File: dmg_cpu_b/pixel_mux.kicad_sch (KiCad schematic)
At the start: 50 parts

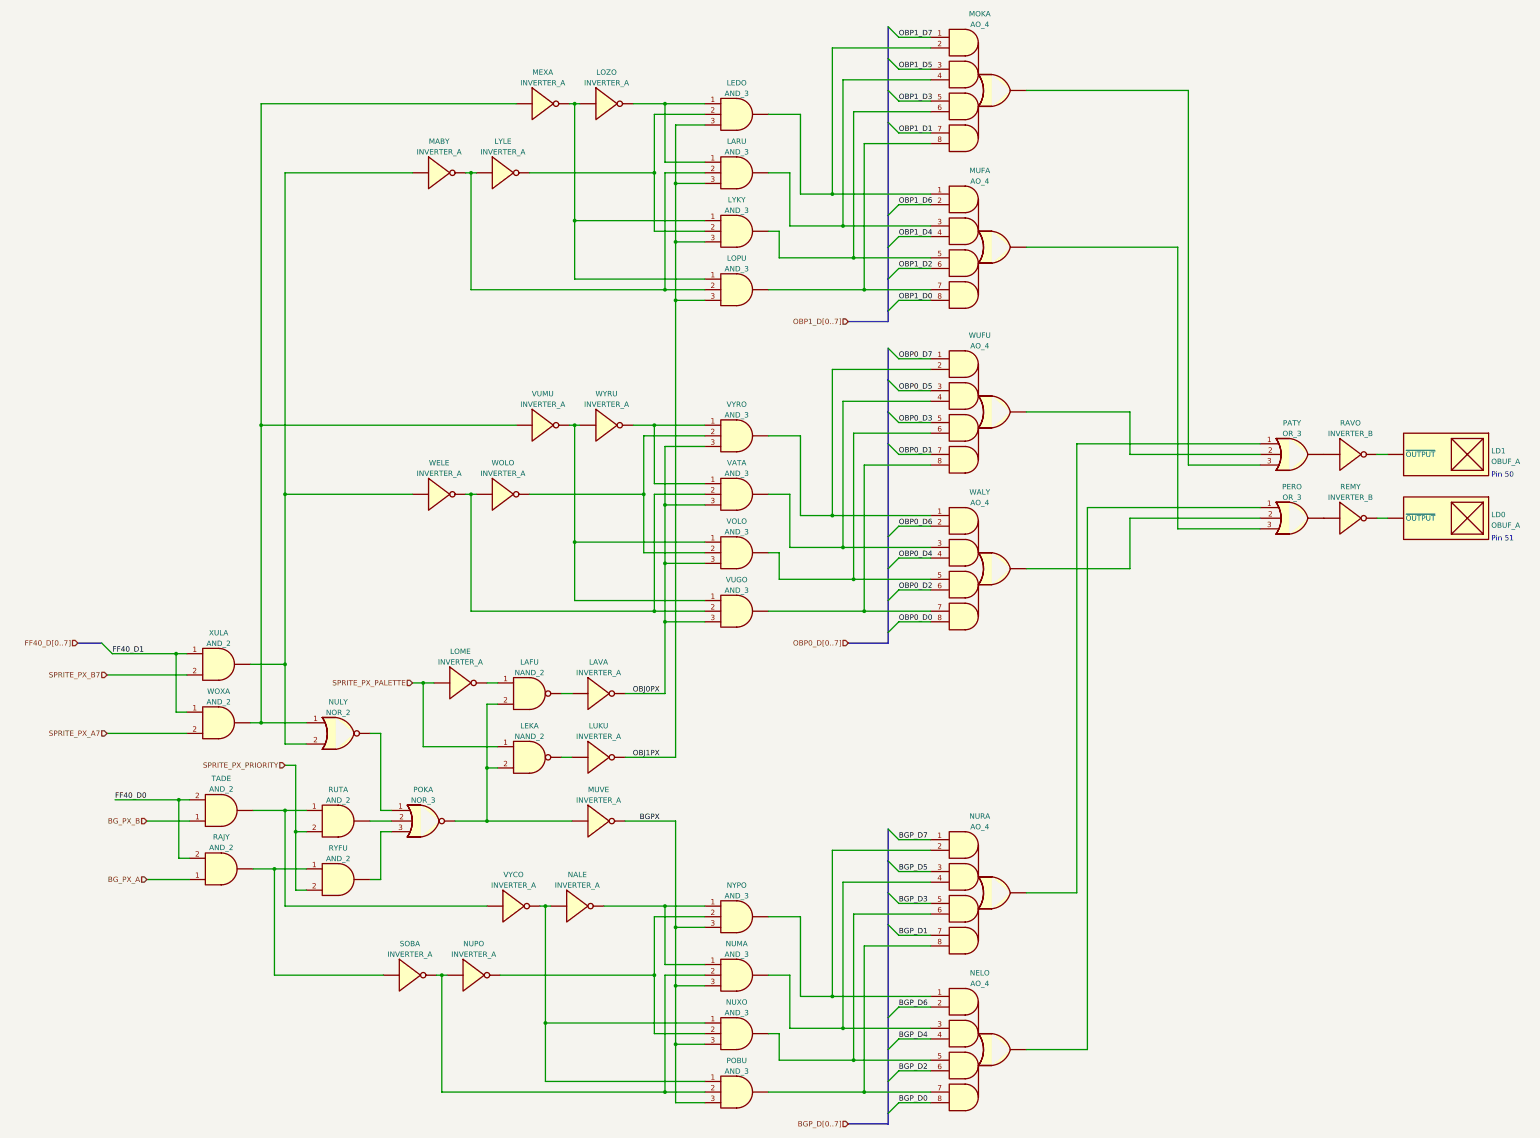
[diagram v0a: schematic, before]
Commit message: Give more meaningful names to cell types
Before this commit, many of the cells types in the chip were named in a
sloppy manner. The different inverter, latch and flip flop valiants were
just suffixed with A, B, C, D, ... Those suffixes gave no information
about the actual differences. They had to be looked up in the
documentation. Now the names of cell types with different variants have
changed:

* Inverter types are named NOT_X1, NOT_X2, NOT_X3, ... The _Xn suffix
  reflects the drive strength of the cell. X1 is the drive strength of
  the weakest inverter, X2 is double the drive strength of the weakest
  inverter.
* Flip flop types are named DFFR, DFFR_CC, DFFR_CC_Q. DFFR is a normal
  data flip flop with reset and a single clock input. The suffix _CC is
  added to flip flops that have two complementary clock inputs (CLK and
  /CLK). Flip flops that only have the positive Q output are suffixed
  with _Q.
* Latch types are named similar to flip flops: DLATCH, DLATCH_EE,
  DLATCH_EE_Q. The suffix _EE is given to latches that require
  "externally inverted enable" signals (ENA and /ENA).
* I/O pad types all start with PAD_BIDIR, PAD_IN or PAD_OUT. They also
  have suffixes that describe what makes them unique, like _PU for
  pull-ups.

Other minor changes were made to align the names with common naming
schemes of other cell libraries.
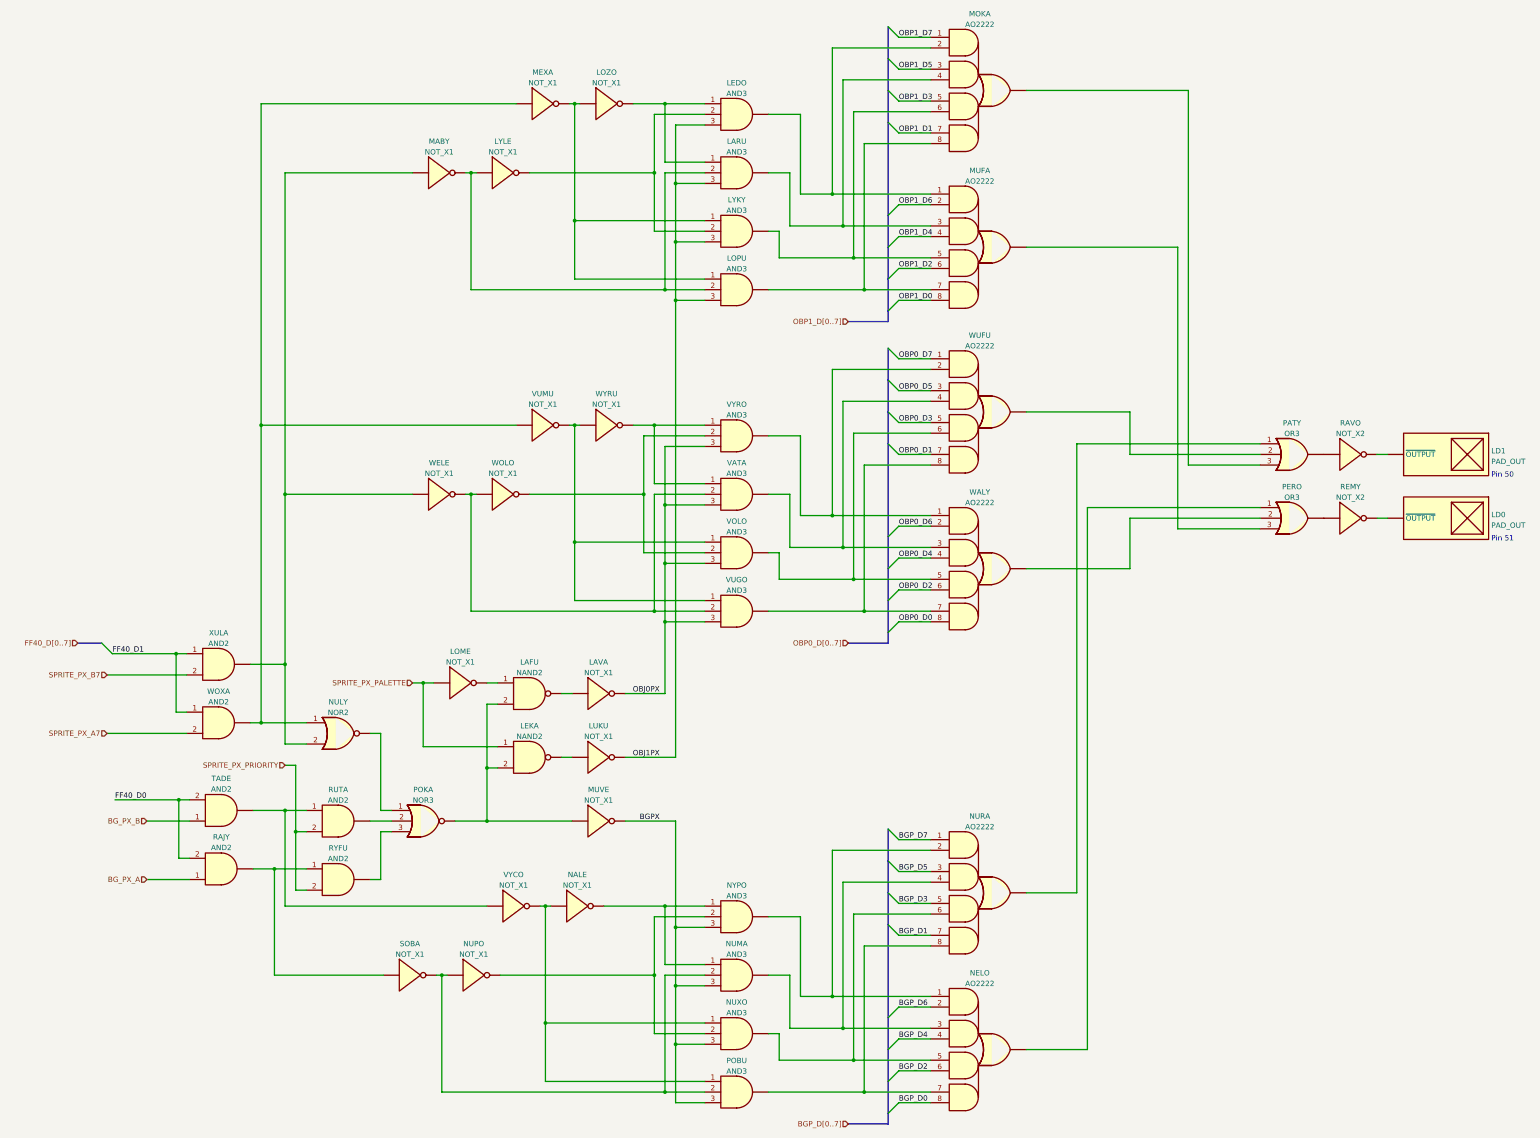
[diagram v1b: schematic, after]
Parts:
- LAFU, LEKA: value NAND_2 -> NAND2; symbol DMG_CPU_Cells:NAND_2 -> DMG_CPU_Cells:NAND2
- LARU, LEDO, LOPU, LYKY, NUMA, NUXO, NYPO, POBU, VATA, VOLO, VUGO, VYRO: value AND_3 -> AND3; symbol DMG_CPU_Cells:AND_3 -> DMG_CPU_Cells:AND3
- LAVA, LOME, LOZO, LUKU, LYLE, MABY, MEXA, MUVE, NALE, NUPO, SOBA, VUMU, VYCO, WELE, WOLO, WYRU: value INVERTER_A -> NOT_X1; symbol DMG_CPU_Cells:INVERTER_A -> DMG_CPU_Cells:NOT_X1
- LD0, LD1: value OBUF_A -> PAD_OUT; symbol DMG_CPU_Cells:OBUF_A -> DMG_CPU_Cells:PAD_OUT
- MOKA, MUFA, NELO, NURA, WALY, WUFU: value AO_4 -> AO2222; symbol DMG_CPU_Cells:AO_4 -> DMG_CPU_Cells:AO2222
- NULY: value NOR_2 -> NOR2; symbol DMG_CPU_Cells:NOR_2 -> DMG_CPU_Cells:NOR2
- PATY, PERO: value OR_3 -> OR3; symbol DMG_CPU_Cells:OR_3 -> DMG_CPU_Cells:OR3
- POKA: value NOR_3 -> NOR3; symbol DMG_CPU_Cells:NOR_3 -> DMG_CPU_Cells:NOR3
- RAJY, RUTA, RYFU, TADE, WOXA, XULA: value AND_2 -> AND2; symbol DMG_CPU_Cells:AND_2 -> DMG_CPU_Cells:AND2
- RAVO, REMY: value INVERTER_B -> NOT_X2; symbol DMG_CPU_Cells:INVERTER_B -> DMG_CPU_Cells:NOT_X2

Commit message: SM83 Layout: Add bottom part of sequencer cells
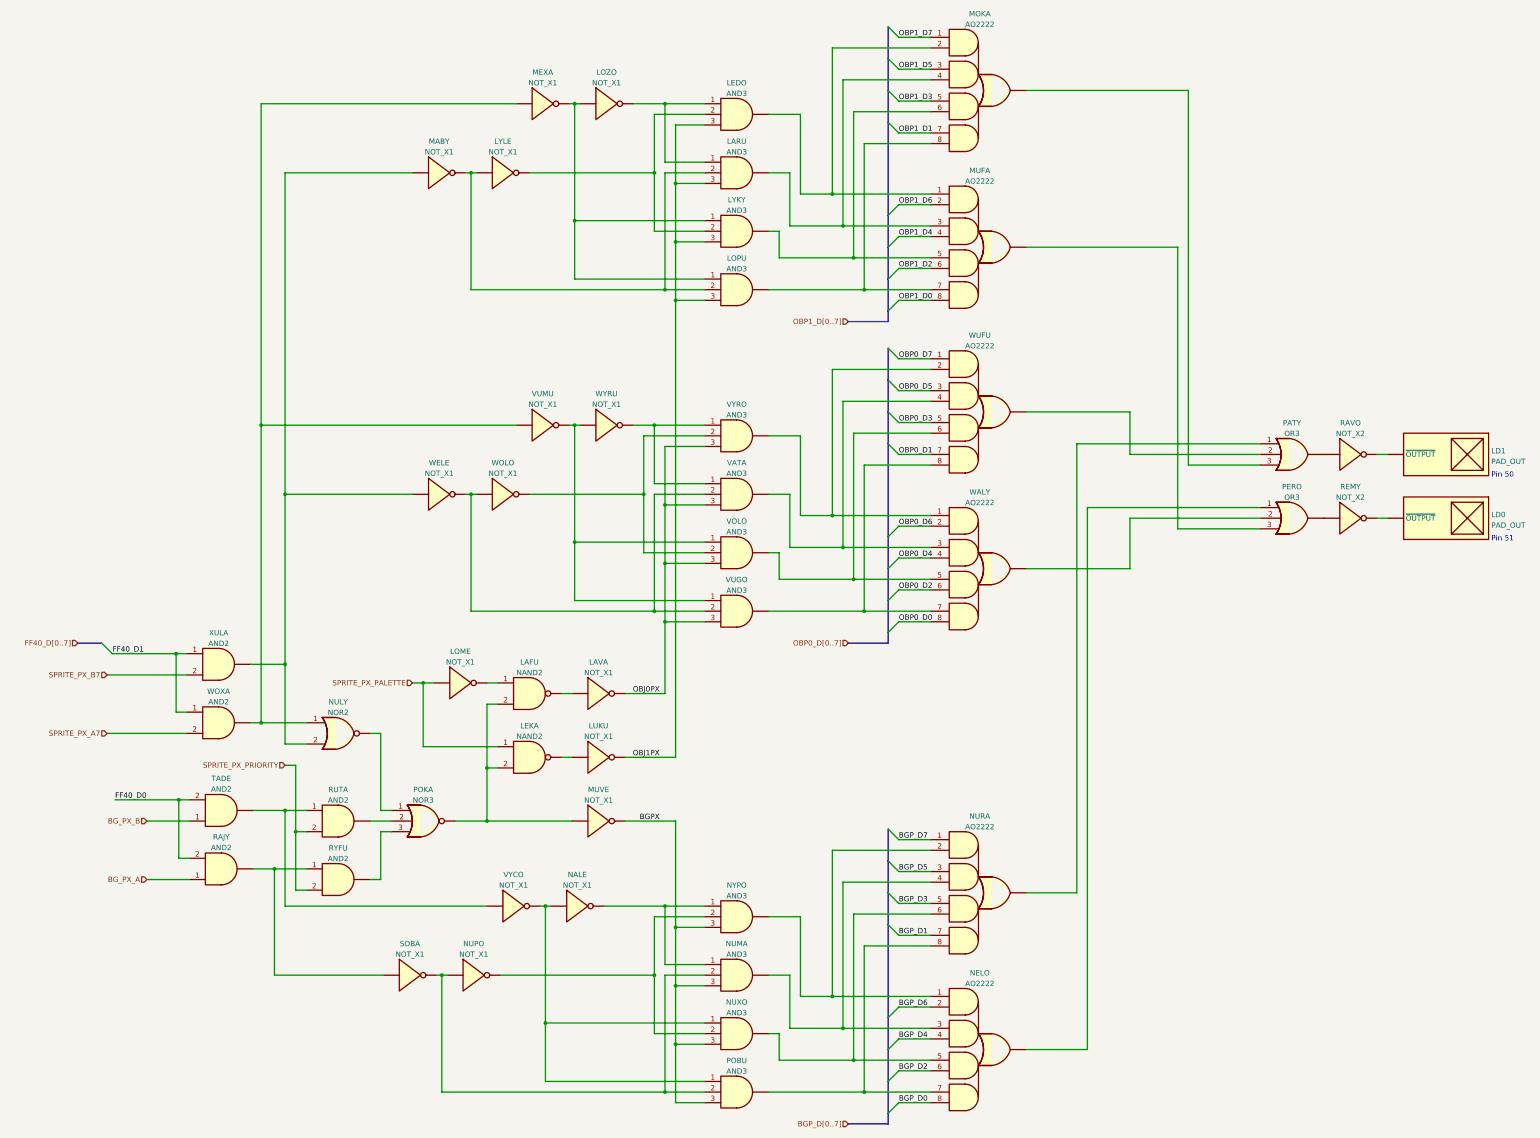
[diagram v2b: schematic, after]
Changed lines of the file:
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@@
 (kicad_sch
-	(version 20231120)
+	(version 20250114)
 	(generator "eeschema")
-	(generator_version "8.0")
+	(generator_version "9.0")
 	(paper "A3")
 	(title_block
 		(title "DMG-CPU B")
-		(date "2025-04-12")
+		(date "2025-04-22")
 		(rev "0.7")
 		(company "CC-BY-SA-4.0 Régis Galland & Michael Singer -- Derived work from Furrtek")
 		(comment 1 "https://github.com/msinger/dmg-schematics")
 	)
+	(text "Pin 51"
+		(exclude_from_sim no)
+		(at 380.365 140.97 0)
+		(effects
+			(font
+				(size 1.27 1.27)
+			)
+			(justify left bottom)
+		)
+	)
+	(text "Pin 50"
+		(exclude_from_sim no)
+		(at 380.365 125.73 0)
+		(effects
+			(font
+				(size 1.27 1.27)
+			)
+			(justify left bottom)
+		)
+	)
 	(junction
 		(at 230.505 80.645)
@@
 		)
 	)
-	(text "Pin 51"
-		(exclude_from_sim no)
-		(at 380.365 140.97 0)
-		(effects
-			(font
-				(size 1.27 1.27)
-			)
-			(justify left bottom)
-		)
-	)
-	(text "Pin 50"
-		(exclude_from_sim no)
-		(at 380.365 125.73 0)
-		(effects
-			(font
-				(size 1.27 1.27)
-			)
-			(justify left bottom)
-		)
-	)
